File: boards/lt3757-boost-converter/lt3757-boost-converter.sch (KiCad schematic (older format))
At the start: 3 parts, among them P1 Enable, P2 BAT IN, P3 24V OUT

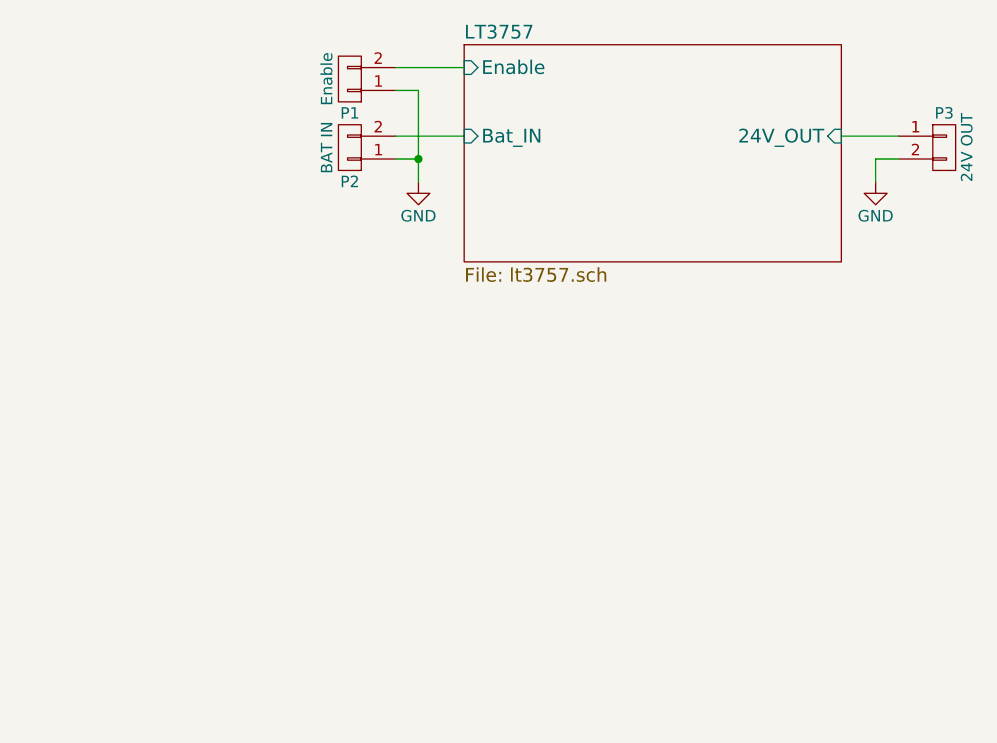
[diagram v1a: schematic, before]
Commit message: [lt3757-boost-converter] remove back side copper
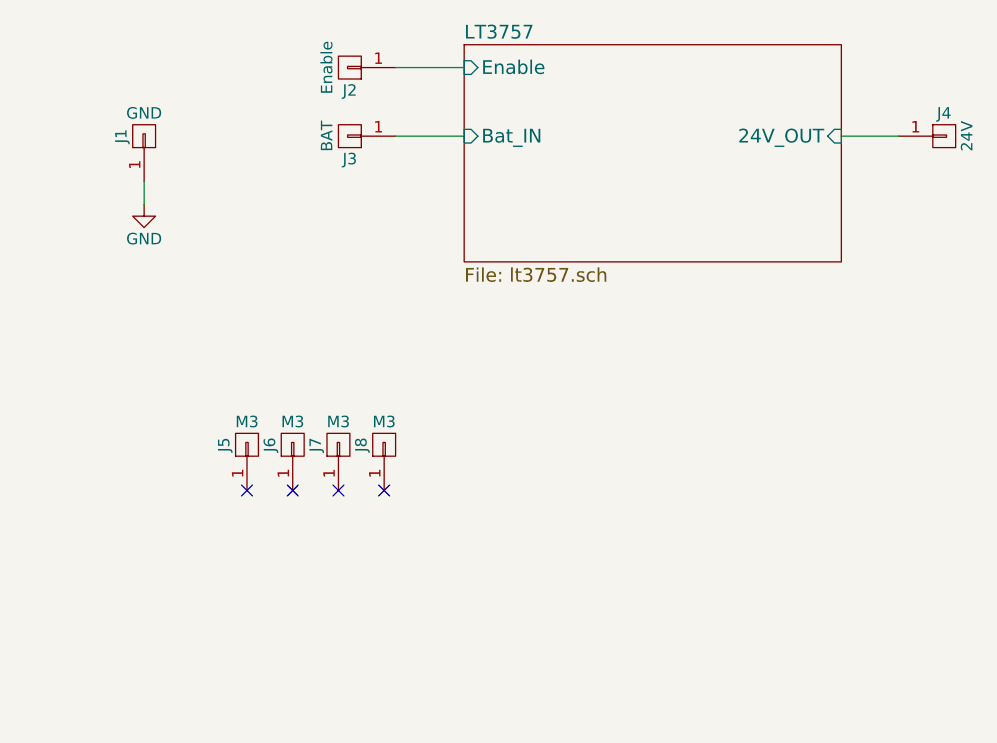
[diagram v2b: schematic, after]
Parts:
- removed P1: Enable, Pin_Headers:Pin_Header_Straight_1x02, symbol CONN_01X02
- removed P2: BAT IN, Connect:bornier2, symbol CONN_01X02
- removed P3: 24V OUT, Connect:bornier2, symbol CONN_01X02
- added J1: GND, Mounting_Holes:MountingHole_3.2mm_M3_Pad, symbol CONN_01X01
- added J2: Enable, Measurement_Points:Measurement_Point_Round-SMD-Pad_Small, symbol CONN_01X01
- added J3: BAT, Mounting_Holes:MountingHole_3.2mm_M3_Pad, symbol CONN_01X01
- added J4: 24V, Mounting_Holes:MountingHole_3.2mm_M3_Pad, symbol CONN_01X01
- added J5, J6, J7, J8: M3, Mounting_Holes:MountingHole_3.2mm_M3_Pad, symbol CONN_01X01
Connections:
- net GND: now also J1.1 (P1)
- net LT3757/24V_OUT: now also J4.1 (P1)
- net LT3757/Bat_IN: now also J3.1 (P1)
- net LT3757/Enable: now also J2.1 (P1)
- no-connect marks 0 -> 4
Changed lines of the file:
@@
 $EndDescr
-$Comp
-L CONN_01X02 P2
-U 1 1 588F8DF1
-P 3950 3750
-F 0 "P2" H 3950 3900 50  0000 C CNN
-F 1 "BAT IN" V 4050 3750 50  0000 C CNN
-F 2 "Connect:bornier2" H 3950 3750 50  0001 C CNN
-F 3 "" H 3950 3750 50  0000 C CNN
-	1    3950 3750
-	-1   0    0    1
-$EndComp
-$Comp
-L CONN_01X02 P3
-U 1 1 588F8E73
-P 6550 3750
-F 0 "P3" H 6550 3900 50  0000 C CNN
-F 1 "24V OUT" V 6650 3750 50  0000 C CNN
-F 2 "Connect:bornier2" H 6550 3750 50  0001 C CNN
-F 3 "" H 6550 3750 50  0000 C CNN
-	1    6550 3750
-	1    0    0    -1
-$EndComp
-$Comp
-L GND #PWR2
-U 1 1 588F8FEC
-P 6250 3900
-F 0 "#PWR2" H 6250 3650 50  0001 C CNN
-F 1 "GND" H 6250 3750 50  0000 C CNN
-F 2 "" H 6250 3900 50  0000 C CNN
-F 3 "" H 6250 3900 50  0000 C CNN
-	1    6250 3900
-	1    0    0    -1
-$EndComp
 $Comp
 L GND #PWR1
 U 1 1 588F9004
-P 4250 3900
-F 0 "#PWR1" H 4250 3650 50  0001 C CNN
-F 1 "GND" H 4250 3750 50  0000 C CNN
-F 2 "" H 4250 3900 50  0000 C CNN
-F 3 "" H 4250 3900 50  0000 C CNN
-	1    4250 3900
+P 3050 4000
+F 0 "#PWR1" H 3050 3750 50  0001 C CNN
+F 1 "GND" H 3050 3850 50  0000 C CNN
+F 2 "" H 3050 4000 50  0000 C CNN
+F 3 "" H 3050 4000 50  0000 C CNN
+	1    3050 4000
 	1    0    0    -1
 $EndComp
-Wire Wire Line
-	4150 3800 4250 3800
-Wire Wire Line
-	4250 3500 4250 3900
-Wire Wire Line
-	6250 3900 6250 3800
-Wire Wire Line
-	6250 3800 6350 3800
 $Sheet
 S 4450 3300 1650 950
@@
 F4 "Enable" I L 4450 3400 60
 $EndSheet
-$Comp
-L CONN_01X02 P1
-U 1 1 588F9182
-P 3950 3450
-F 0 "P1" H 3950 3600 50  0000 C CNN
-F 1 "Enable" V 4050 3450 50  0000 C CNN
-F 2 "Pin_Headers:Pin_Header_Straight_1x02" H 3950 3450 50  0001 C CNN
-F 3 "" H 3950 3450 50  0000 C CNN
-	1    3950 3450
-	-1   0    0    1
-$EndComp
 Wire Wire Line
 	4150 3700 4450 3700
@@
 	4450 3400 4150 3400
 Wire Wire Line
-	4150 3500 4250 3500
-Connection ~ 4250 3800
+	6350 3700 6100 3700
+$Comp
+L CONN_01X01 J1
+U 1 1 5947E114
+P 3050 3700
+F 0 "J1" H 3050 3800 50  0000 C CNN
+F 1 "GND" V 3150 3700 50  0000 C CNN
+F 2 "Mounting_Holes:MountingHole_3.2mm_M3_Pad" H 3050 3700 50  0001 C CNN
+F 3 "" H 3050 3700 50  0001 C CNN
+	1    3050 3700
+	0    -1   -1   0
+$EndComp
 Wire Wire Line
-	6350 3700 6100 3700
+	3050 3900 3050 4000
+$Comp
+L CONN_01X01 J2
+U 1 1 5947E36C
+P 3950 3400
+F 0 "J2" H 3950 3500 50  0000 C CNN
+F 1 "Enable" V 4050 3400 50  0000 C CNN
+F 2 "Measurement_Points:Measurement_Point_Round-SMD-Pad_Small" H 3950 3400 50  0001 C CNN
+F 3 "" H 3950 3400 50  0001 C CNN
+	1    3950 3400
+	-1   0    0    1
+$EndComp
+$Comp
+L CONN_01X01 J3
+U 1 1 5947E41A
+P 3950 3700
+F 0 "J3" H 3950 3800 50  0000 C CNN
+F 1 "BAT" V 4050 3700 50  0000 C CNN
+F 2 "Mounting_Holes:MountingHole_3.2mm_M3_Pad" H 3950 3700 50  0001 C CNN
+F 3 "" H 3950 3700 50  0001 C CNN
+	1    3950 3700
+	-1   0    0    1
+$EndComp
+$Comp
+L CONN_01X01 J4
+U 1 1 5947E508
+P 6550 3700
+F 0 "J4" H 6550 3800 50  0000 C CNN
+F 1 "24V" V 6650 3700 50  0000 C CNN
+F 2 "Mounting_Holes:MountingHole_3.2mm_M3_Pad" H 6550 3700 50  0001 C CNN
+F 3 "" H 6550 3700 50  0001 C CNN
+	1    6550 3700
+	1    0    0    -1
+$EndComp
+$Comp
+L CONN_01X01 J5
+U 1 1 59480535
+P 3500 5050
+F 0 "J5" H 3500 5150 50  0000 C CNN
+F 1 "M3" V 3600 5050 50  0000 C CNN
+F 2 "Mounting_Holes:MountingHole_3.2mm_M3_Pad" H 3500 5050 50  0001 C CNN
+F 3 "" H 3500 5050 50  0001 C CNN
+	1    3500 5050
+	0    -1   -1   0
+$EndComp
+$Comp
+L CONN_01X01 J6
+U 1 1 594806B2
+P 3700 5050
+F 0 "J6" H 3700 5150 50  0000 C CNN
+F 1 "M3" V 3800 5050 50  0000 C CNN
+F 2 "Mounting_Holes:MountingHole_3.2mm_M3_Pad" H 3700 5050 50  0001 C CNN
+F 3 "" H 3700 5050 50  0001 C CNN
+	1    3700 5050
+	0    -1   -1   0
+$EndComp
+$Comp
+L CONN_01X01 J7
+U 1 1 594806EE
+P 3900 5050
+F 0 "J7" H 3900 5150 50  0000 C CNN
+F 1 "M3" V 4000 5050 50  0000 C CNN
+F 2 "Mounting_Holes:MountingHole_3.2mm_M3_Pad" H 3900 5050 50  0001 C CNN
+F 3 "" H 3900 5050 50  0001 C CNN
+	1    3900 5050
+	0    -1   -1   0
+$EndComp
+$Comp
+L CONN_01X01 J8
+U 1 1 59480729
+P 4100 5050
+F 0 "J8" H 4100 5150 50  0000 C CNN
+F 1 "M3" V 4200 5050 50  0000 C CNN
+F 2 "Mounting_Holes:MountingHole_3.2mm_M3_Pad" H 4100 5050 50  0001 C CNN
+F 3 "" H 4100 5050 50  0001 C CNN
+	1    4100 5050
+	0    -1   -1   0
+$EndComp
+NoConn ~ 3500 5250
+NoConn ~ 3700 5250
+NoConn ~ 3900 5250
+NoConn ~ 4100 5250
 $EndSCHEMATC

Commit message: [lt3757-boost-converter] finish single-sided layout for IMS PCB
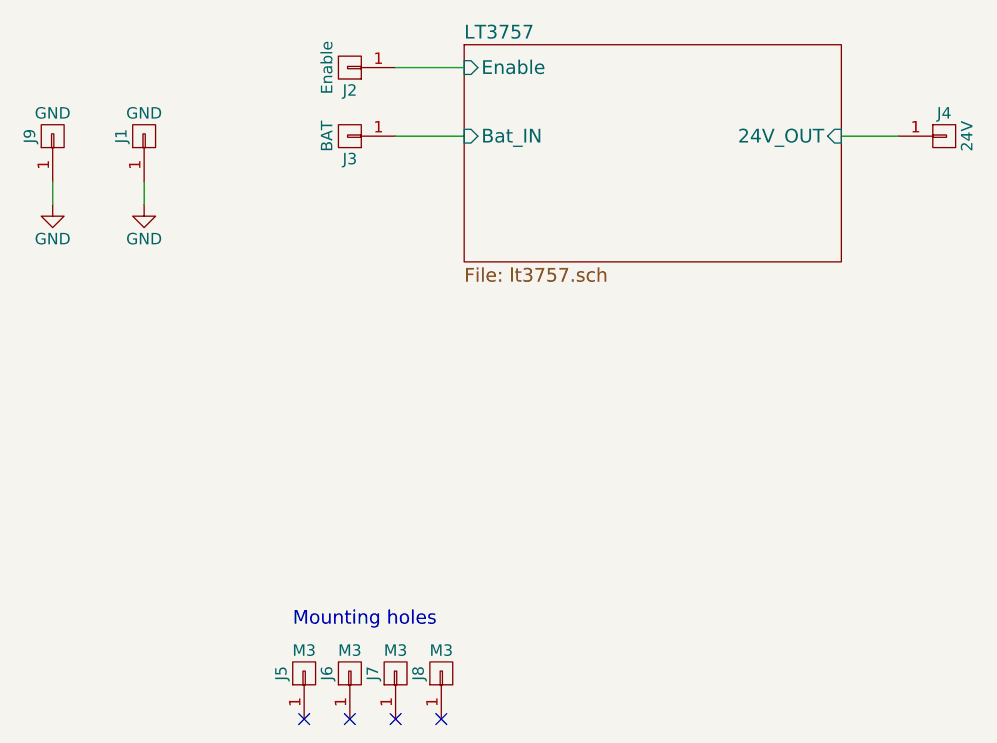
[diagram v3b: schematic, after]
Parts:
- added J9: GND, Mounting_Holes:MountingHole_3.2mm_M3_Pad, symbol CONN_01X01
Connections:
- net GND: now also J9.1 (P1)
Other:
- note added: "Mounting holes"
- moved on the sheet: J5, J6, J7, J8
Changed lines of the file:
@@
 $EndDescr
 $Comp
-L GND #PWR1
+L GND #PWR2
 U 1 1 588F9004
 P 3050 4000
-F 0 "#PWR1" H 3050 3750 50  0001 C CNN
+F 0 "#PWR2" H 3050 3750 50  0001 C CNN
 F 1 "GND" H 3050 3850 50  0000 C CNN
 F 2 "" H 3050 4000 50  0000 C CNN
@@
 L CONN_01X01 J5
 U 1 1 59480535
-P 3500 5050
-F 0 "J5" H 3500 5150 50  0000 C CNN
-F 1 "M3" V 3600 5050 50  0000 C CNN
-F 2 "Mounting_Holes:MountingHole_3.2mm_M3_Pad" H 3500 5050 50  0001 C CNN
-F 3 "" H 3500 5050 50  0001 C CNN
-	1    3500 5050
+P 3750 6050
+F 0 "J5" H 3750 6150 50  0000 C CNN
+F 1 "M3" V 3850 6050 50  0000 C CNN
+F 2 "Mounting_Holes:MountingHole_3.2mm_M3_Pad" H 3750 6050 50  0001 C CNN
+F 3 "" H 3750 6050 50  0001 C CNN
+	1    3750 6050
 	0    -1   -1   0
 $EndComp
@@
 L CONN_01X01 J6
 U 1 1 594806B2
-P 3700 5050
-F 0 "J6" H 3700 5150 50  0000 C CNN
-F 1 "M3" V 3800 5050 50  0000 C CNN
-F 2 "Mounting_Holes:MountingHole_3.2mm_M3_Pad" H 3700 5050 50  0001 C CNN
-F 3 "" H 3700 5050 50  0001 C CNN
-	1    3700 5050
+P 3950 6050
+F 0 "J6" H 3950 6150 50  0000 C CNN
+F 1 "M3" V 4050 6050 50  0000 C CNN
+F 2 "Mounting_Holes:MountingHole_3.2mm_M3_Pad" H 3950 6050 50  0001 C CNN
+F 3 "" H 3950 6050 50  0001 C CNN
+	1    3950 6050
 	0    -1   -1   0
 $EndComp
@@
 L CONN_01X01 J7
 U 1 1 594806EE
-P 3900 5050
-F 0 "J7" H 3900 5150 50  0000 C CNN
-F 1 "M3" V 4000 5050 50  0000 C CNN
-F 2 "Mounting_Holes:MountingHole_3.2mm_M3_Pad" H 3900 5050 50  0001 C CNN
-F 3 "" H 3900 5050 50  0001 C CNN
-	1    3900 5050
+P 4150 6050
+F 0 "J7" H 4150 6150 50  0000 C CNN
+F 1 "M3" V 4250 6050 50  0000 C CNN
+F 2 "Mounting_Holes:MountingHole_3.2mm_M3_Pad" H 4150 6050 50  0001 C CNN
+F 3 "" H 4150 6050 50  0001 C CNN
+	1    4150 6050
 	0    -1   -1   0
 $EndComp
@@
 L CONN_01X01 J8
 U 1 1 59480729
-P 4100 5050
-F 0 "J8" H 4100 5150 50  0000 C CNN
-F 1 "M3" V 4200 5050 50  0000 C CNN
-F 2 "Mounting_Holes:MountingHole_3.2mm_M3_Pad" H 4100 5050 50  0001 C CNN
-F 3 "" H 4100 5050 50  0001 C CNN
-	1    4100 5050
+P 4350 6050
+F 0 "J8" H 4350 6150 50  0000 C CNN
+F 1 "M3" V 4450 6050 50  0000 C CNN
+F 2 "Mounting_Holes:MountingHole_3.2mm_M3_Pad" H 4350 6050 50  0001 C CNN
+F 3 "" H 4350 6050 50  0001 C CNN
+	1    4350 6050
 	0    -1   -1   0
 $EndComp
-NoConn ~ 3500 5250
-NoConn ~ 3700 5250
-NoConn ~ 3900 5250
-NoConn ~ 4100 5250
+NoConn ~ 3750 6250
+NoConn ~ 3950 6250
+NoConn ~ 4150 6250
+NoConn ~ 4350 6250
+$Comp
+L GND #PWR1
+U 1 1 594829D4
+P 2650 4000
+F 0 "#PWR1" H 2650 3750 50  0001 C CNN
+F 1 "GND" H 2650 3850 50  0000 C CNN
+F 2 "" H 2650 4000 50  0000 C CNN
+F 3 "" H 2650 4000 50  0000 C CNN
+	1    2650 4000
+	1    0    0    -1
+$EndComp
+$Comp
+L CONN_01X01 J9
+U 1 1 594829DA
+P 2650 3700
+F 0 "J9" H 2650 3800 50  0000 C CNN
+F 1 "GND" V 2750 3700 50  0000 C CNN
+F 2 "Mounting_Holes:MountingHole_3.2mm_M3_Pad" H 2650 3700 50  0001 C CNN
+F 3 "" H 2650 3700 50  0001 C CNN
+	1    2650 3700
+	0    -1   -1   0
+$EndComp
+Wire Wire Line
+	2650 3900 2650 4000
+Text Notes 3700 5850 0    60   ~ 0
+Mounting holes
 $EndSCHEMATC
